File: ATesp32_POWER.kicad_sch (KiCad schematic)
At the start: 17 parts, among them J1 USB_C_Receptacle_USB2.0_16P, J2 JST PH, Q1 DMP2045U, U3 MCP73831-2-OT, U4 AP2112K-3.3

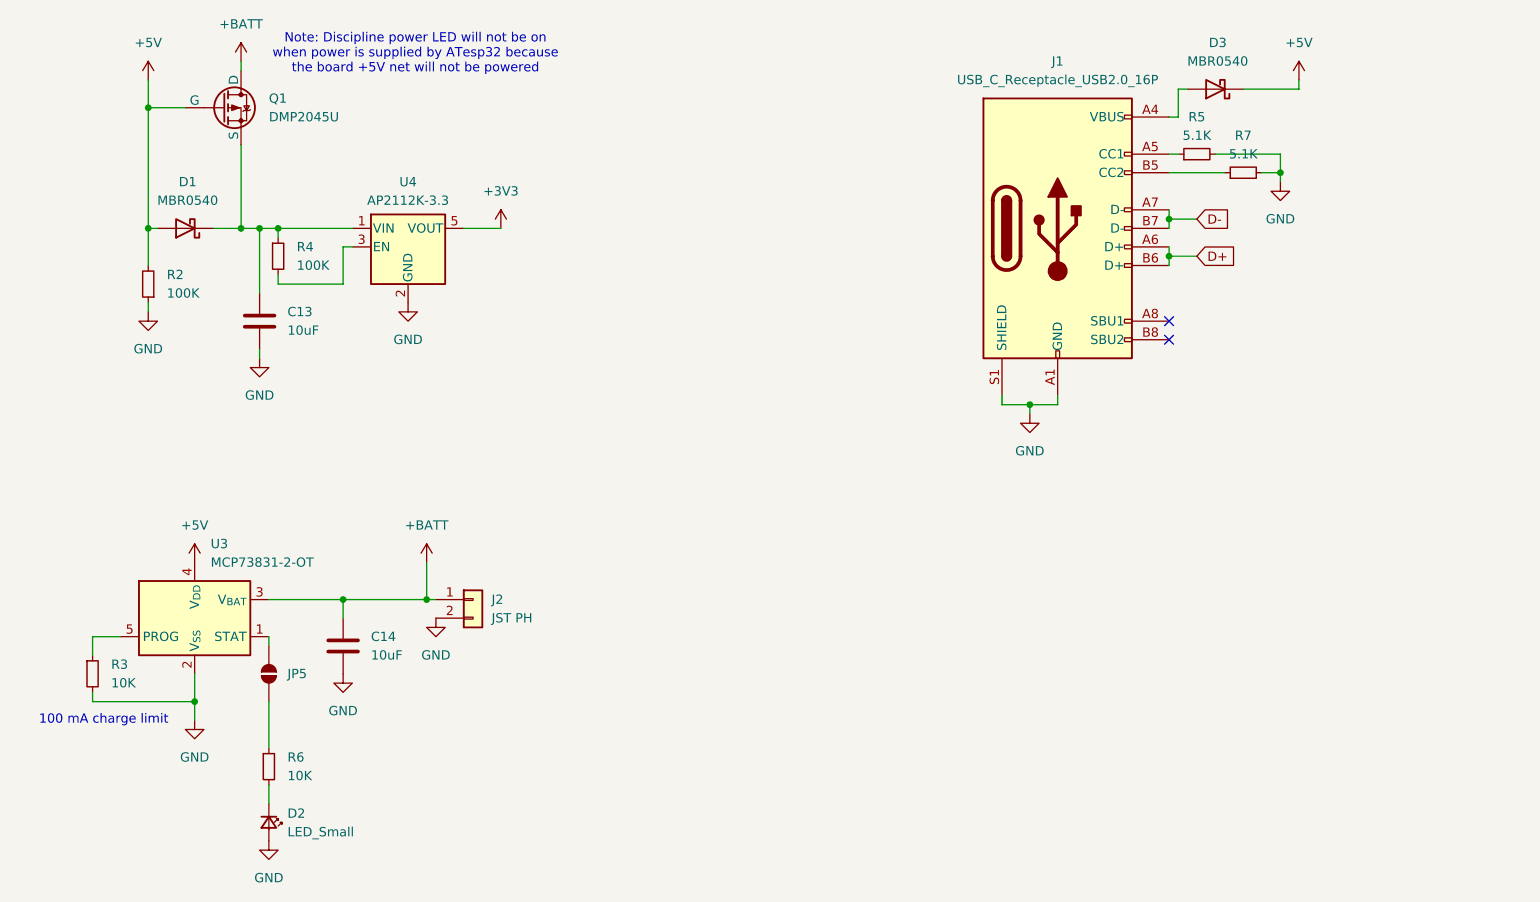
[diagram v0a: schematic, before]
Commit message: Added USB-UART bridge for programming
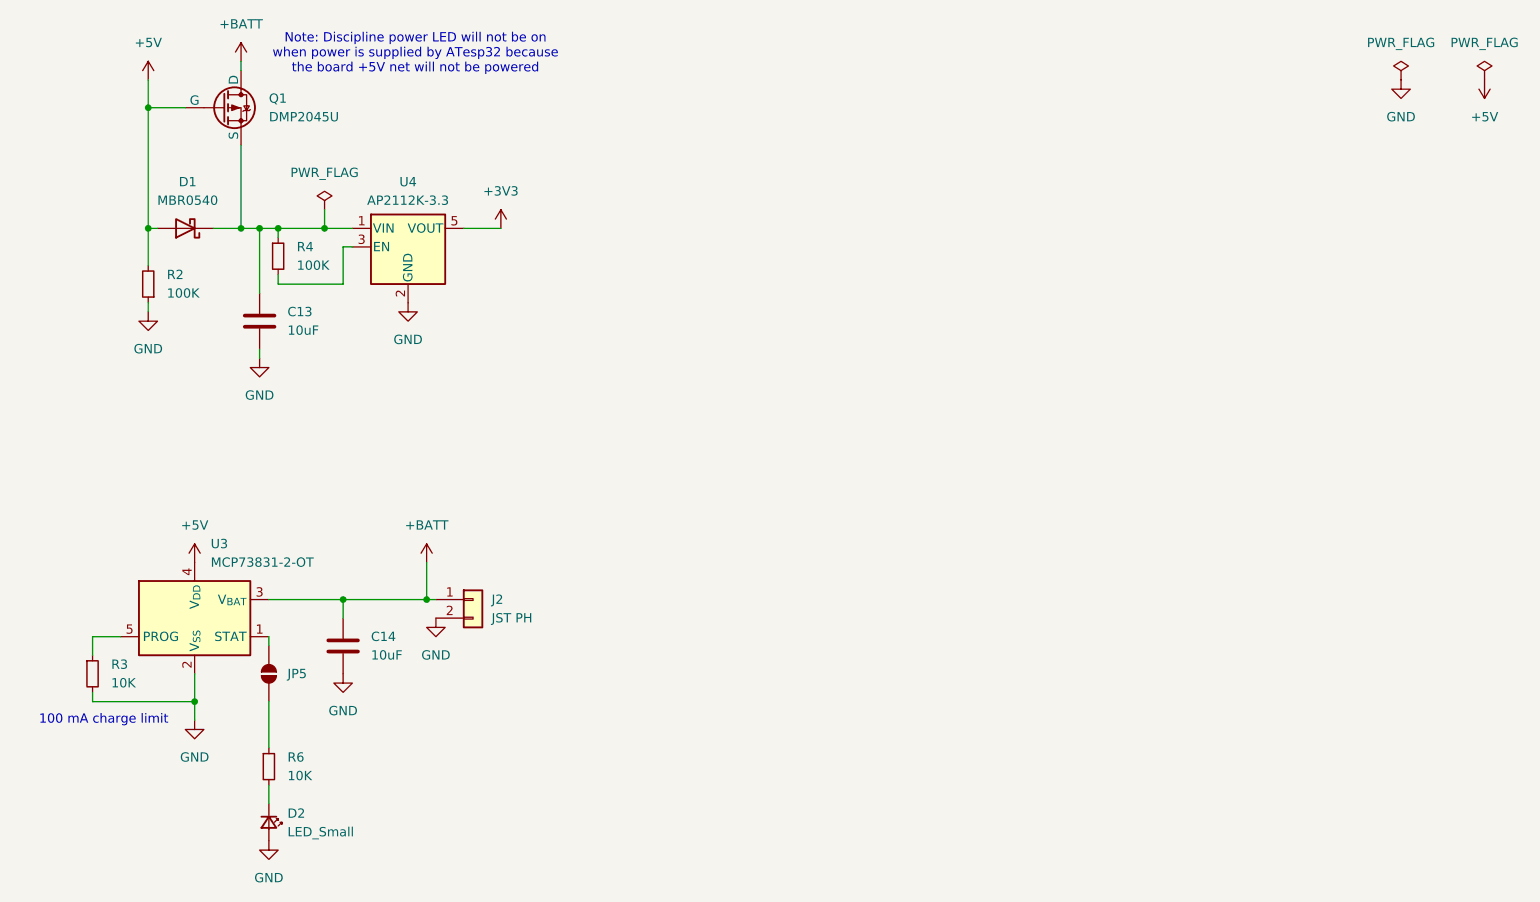
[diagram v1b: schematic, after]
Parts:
- removed D3: MBR0540, Diode_SMD:D_SOD-123, symbol Diode:MBR0540
- removed J1: USB_C_Receptacle_USB2.0_16P, symbol Connector:USB_C_Receptacle_USB2.0_16P
- removed R5, R7: 5.1K, symbol Device:R_Small
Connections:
- no-connect marks 2 -> 0

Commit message: first pass at footprint assignment
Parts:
- C13, C14: footprint (none) -> Capacitor_SMD:C_0603_1608Metric
- D2: footprint (none) -> LED_SMD:LED_0603_1608Metric
- J2: footprint (none) -> Connector_JST:JST_PH_B2B-PH-K_1x02_P2.00mm_Vertical
- JP5: footprint (none) -> Jumper:SolderJumper-2_P1.3mm_Open_RoundedPad1.0x1.5mm
- Q1: footprint (none) -> Package_TO_SOT_SMD:SOT-23
- R2, R3, R4, R6: footprint (none) -> Resistor_SMD:R_0603_1608Metric
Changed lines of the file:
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@@
 			)
 		)
-		(property "Footprint" ""
+		(property "Footprint" "LED_SMD:LED_0603_1608Metric"
 			(at 99.06 152.4 90)
 			(effects
@@
 			)
 		)
-		(property "Footprint" ""
+		(property "Footprint" "Capacitor_SMD:C_0603_1608Metric"
 			(at 98.7552 87.63 0)
 			(effects
@@
 			)
 		)
-		(property "Footprint" ""
+		(property "Footprint" "Capacitor_SMD:C_0603_1608Metric"
 			(at 110.1852 132.08 0)
 			(effects
@@
 			)
 		)
-		(property "Footprint" ""
+		(property "Footprint" "Resistor_SMD:R_0603_1608Metric"
 			(at 99.06 144.78 0)
 			(effects
@@
 			)
 		)
-		(property "Footprint" ""
+		(property "Footprint" "Resistor_SMD:R_0603_1608Metric"
 			(at 74.93 132.08 0)
 			(effects
@@
 			)
 		)
-		(property "Footprint" ""
+		(property "Footprint" "Jumper:SolderJumper-2_P1.3mm_Open_RoundedPad1.0x1.5mm"
 			(at 99.06 132.08 0)
 			(effects
@@
 			)
 		)
-		(property "Footprint" ""
+		(property "Footprint" "Resistor_SMD:R_0603_1608Metric"
 			(at 100.33 74.93 0)
 			(effects
@@
 			)
 		)
-		(property "Footprint" ""
+		(property "Footprint" "Resistor_SMD:R_0603_1608Metric"
 			(at 82.55 78.74 0)
 			(effects
@@
 			)
 		)
-		(property "Footprint" ""
+		(property "Footprint" "Connector_JST:JST_PH_B2B-PH-K_1x02_P2.00mm_Vertical"
 			(at 127 121.92 0)
 			(effects
@@
 			)
 		)
-		(property "Footprint" ""
+		(property "Footprint" "Package_TO_SOT_SMD:SOT-23"
 			(at 97.79 52.07 0)
 			(effects

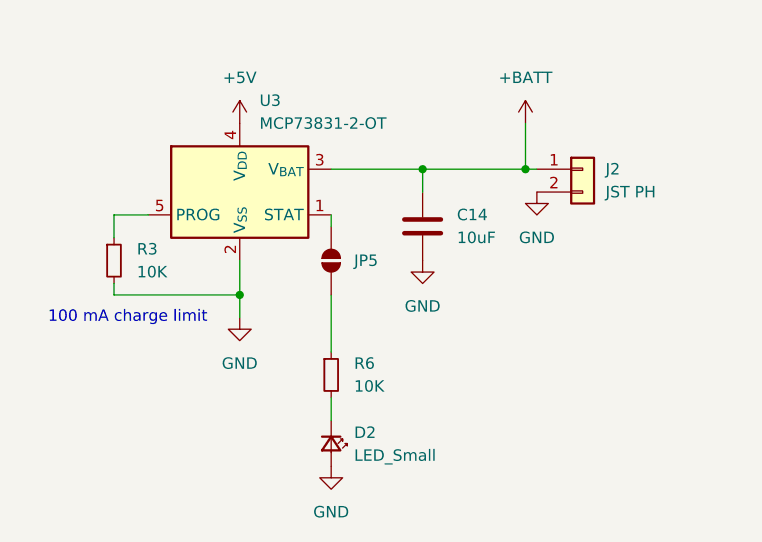
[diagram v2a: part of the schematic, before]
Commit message: remove misc superfluous components
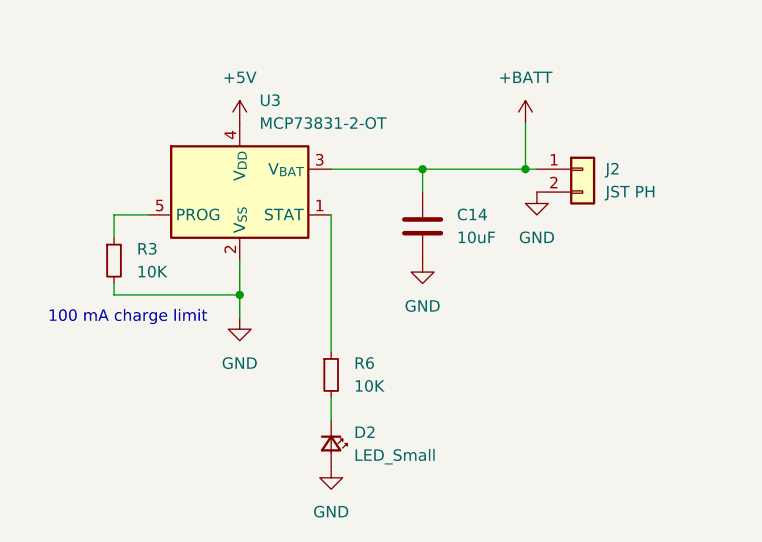
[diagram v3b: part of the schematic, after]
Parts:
- removed JP5: SolderJumper_2_Open, Jumper:SolderJumper-2_P1.3mm_Open_RoundedPad1.0x1.5mm, symbol Jumper:SolderJumper_2_Open
- C13, C14: footprint Capacitor_SMD:C_0603_1608Metric -> Capacitor_SMD:C_0402_1005Metric
- D2: footprint LED_SMD:LED_0603_1608Metric -> LED_SMD:LED_0402_1005Metric
- J2: footprint Connector_JST:JST_PH_B2B-PH-K_1x02_P2.00mm_Vertical -> Connector_JST:JST_PH_S2B-PH-SM4-TB_1x02-1MP_P2.00mm_Horizontal
- R2, R3, R4, R6: footprint Resistor_SMD:R_0603_1608Metric -> Resistor_SMD:R_0402_1005Metric
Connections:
- net at R6.1: now also U3.1 (STAT)
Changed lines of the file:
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@@
 	(wire
 		(pts
-			(xy 99.06 127) (xy 99.06 128.27)
+			(xy 82.55 54.61) (xy 82.55 71.12)
 		)
 		(stroke
@@
 	(wire
 		(pts
-			(xy 82.55 54.61) (xy 82.55 71.12)
-		)
-		(stroke
-			(width 0)
-			(type default)
-		)
-	)
-	(wire
-		(pts
-			(xy 99.06 135.89) (xy 99.06 142.24)
+			(xy 99.06 127) (xy 99.06 142.24)
 		)
 		(stroke
@@
 			)
 		)
-		(property "Footprint" "LED_SMD:LED_0603_1608Metric"
+		(property "Footprint" "LED_SMD:LED_0402_1005Metric"
 			(at 99.06 152.4 90)
 			(effects
@@
 			)
 		)
-		(property "Footprint" "Capacitor_SMD:C_0603_1608Metric"
+		(property "Footprint" "Capacitor_SMD:C_0402_1005Metric"
 			(at 98.7552 87.63 0)
 			(effects
@@
 			)
 		)
-		(property "Footprint" "Capacitor_SMD:C_0603_1608Metric"
+		(property "Footprint" "Capacitor_SMD:C_0402_1005Metric"
 			(at 110.1852 132.08 0)
 			(effects
@@
 			)
 		)
-		(property "Footprint" "Resistor_SMD:R_0603_1608Metric"
+		(property "Footprint" "Resistor_SMD:R_0402_1005Metric"
 			(at 99.06 144.78 0)
 			(effects
@@
 			)
 		)
-		(property "Footprint" "Resistor_SMD:R_0603_1608Metric"
+		(property "Footprint" "Resistor_SMD:R_0402_1005Metric"
 			(at 74.93 132.08 0)
 			(effects
@@
 	)
 	(symbol
-		(lib_id "Jumper:SolderJumper_2_Open")
-		(at 99.06 132.08 90)
-		(unit 1)
-		(exclude_from_sim yes)
-		(in_bom no)
-		(on_board yes)
-		(dnp no)
-		(fields_autoplaced yes)
-		(property "Reference" "JP5"
-			(at 101.6 132.0799 90)
-			(effects
-				(font
-					(size 1.27 1.27)
-				)
-				(justify right)
-			)
-		)
-		(property "Value" "SolderJumper_2_Open"
-			(at 95.25 132.08 0)
-			(effects
-				(font
-					(size 1.27 1.27)
-				)
-				(hide yes)
-			)
-		)
-		(property "Footprint" "Jumper:SolderJumper-2_P1.3mm_Open_RoundedPad1.0x1.5mm"
-			(at 99.06 132.08 0)
-			(effects
-				(font
-					(size 1.27 1.27)
-				)
-				(hide yes)
-			)
-		)
-		(property "Datasheet" "~"
-			(at 99.06 132.08 0)
-			(effects
-				(font
-					(size 1.27 1.27)
-				)
-				(hide yes)
-			)
-		)
-		(property "Description" "Solder Jumper, 2-pole, open"
-			(at 99.06 132.08 0)
-			(effects
-				(font
-					(size 1.27 1.27)
-				)
-				(hide yes)
-			)
-		)
-		(pin "2"
-		)
-		(pin "1"
-		)
-		(instances
-			(project "ATesp32"
-				(path "/465ced44-ee36-4323-9fa6-a4501ea89ff6/2df8408e-27a9-477c-88a6-1eead4d75269"
-					(reference "JP5")
-					(unit 1)
-				)
-			)
-		)
-	)
-	(symbol
 		(lib_id "power:+5V")
 		(at 88.9 116.84 0)
@@
 			)
 		)
-		(property "Footprint" "Resistor_SMD:R_0603_1608Metric"
+		(property "Footprint" "Resistor_SMD:R_0402_1005Metric"
 			(at 100.33 74.93 0)
 			(effects
@@
 			)
 		)
-		(property "Footprint" "Resistor_SMD:R_0603_1608Metric"
+		(property "Footprint" "Resistor_SMD:R_0402_1005Metric"
 			(at 82.55 78.74 0)
 			(effects
@@
 			)
 		)
-		(property "Footprint" "Connector_JST:JST_PH_B2B-PH-K_1x02_P2.00mm_Vertical"
+		(property "Footprint" "Connector_JST:JST_PH_S2B-PH-SM4-TB_1x02-1MP_P2.00mm_Horizontal"
 			(at 127 121.92 0)
 			(effects

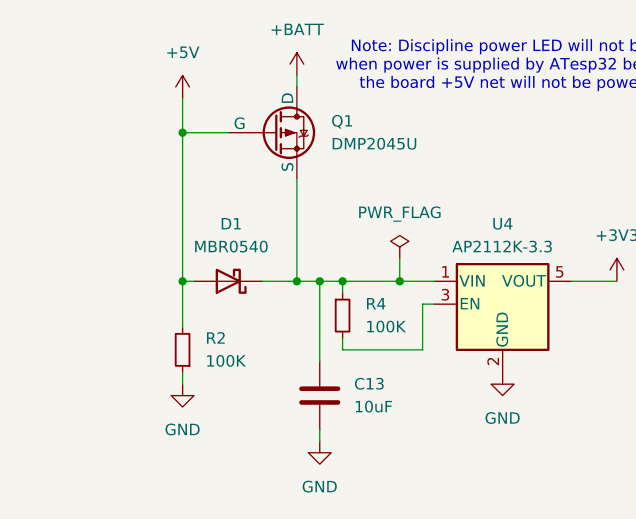
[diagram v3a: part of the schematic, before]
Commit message: first pass at component placement
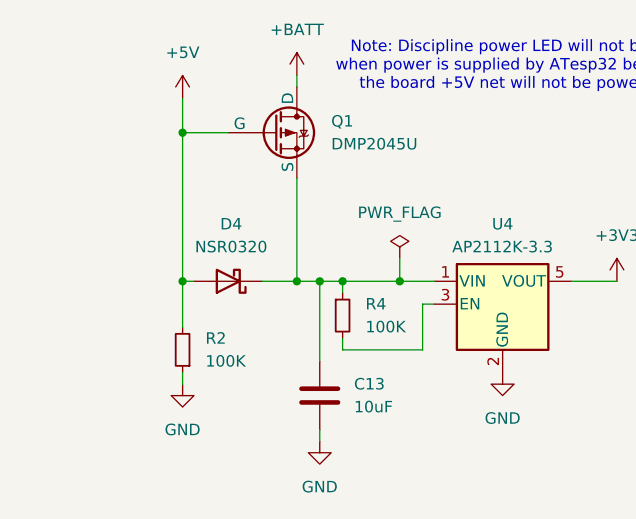
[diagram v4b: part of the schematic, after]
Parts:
- removed D1: MBR0540, Diode_SMD:D_SOD-123, symbol Diode:MBR0540
- added D4: NSR0320, Diode_SMD:D_SOD-323, symbol Diode:NSR0340HT1G
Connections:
- net +5V: now also D4.2 (A)
- net at C13.1, Q1.3 (S), R4.1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: now also D4.1 (K)
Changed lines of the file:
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@@
-	)
-	(symbol
-		(lib_id "Diode:MBR0540")
-		(at 87.63 71.12 180)
-		(unit 1)
-		(exclude_from_sim no)
-		(in_bom yes)
-		(on_board yes)
-		(dnp no)
-		(fields_autoplaced yes)
-		(property "Reference" "D1"
-			(at 87.9475 64.77 0)
-			(effects
-				(font
-					(size 1.27 1.27)
-				)
-			)
-		)
-		(property "Value" "MBR0540"
-			(at 87.9475 67.31 0)
-			(effects
-				(font
-					(size 1.27 1.27)
-				)
-			)
-		)
-		(property "Footprint" "Diode_SMD:D_SOD-123"
-			(at 87.63 66.675 0)
-			(effects
-				(font
-					(size 1.27 1.27)
-				)
-				(hide yes)
-			)
-		)
-		(property "Datasheet" "http://www.mccsemi.com/up_pdf/MBR0520~MBR0580(SOD123).pdf"
-			(at 87.63 71.12 0)
-			(effects
-				(font
-					(size 1.27 1.27)
-				)
-				(hide yes)
-			)
-		)
-		(property "Description" "40V 0.5A Schottky Power Rectifier Diode, SOD-123"
-			(at 87.63 71.12 0)
-			(effects
-				(font
-					(size 1.27 1.27)
-				)
-				(hide yes)
-			)
-		)
-		(pin "1"
-		)
-		(pin "2"
-		)
-		(instances
-			(project "ATesp32"
-				(path "/465ced44-ee36-4323-9fa6-a4501ea89ff6/2df8408e-27a9-477c-88a6-1eead4d75269"
-					(reference "D1")
-					(unit 1)
-				)
-			)
-		)
 	)
 	(symbol
@@
 					(unit 1)
 				)
+			)
+		)
+	)
+	(symbol
+		(lib_id "Diode:NSR0340HT1G")
+		(at 87.63 71.12 180)
+		(unit 1)
+		(exclude_from_sim no)
+		(in_bom yes)
+		(on_board yes)
+		(dnp no)
+		(fields_autoplaced yes)
+		(property "Reference" "D4"
+			(at 87.9475 64.77 0)
+			(effects
+				(font
+					(size 1.27 1.27)
+				)
+			)
+		)
+		(property "Value" "NSR0320"
+			(at 87.9475 67.31 0)
+			(effects
+				(font
+					(size 1.27 1.27)
+				)
+			)
+		)
+		(property "Footprint" "Diode_SMD:D_SOD-323"
+			(at 87.63 66.675 0)
+			(effects
+				(font
+					(size 1.27 1.27)
+				)
+				(hide yes)
+			)
+		)
+		(property "Datasheet" "https://www.onsemi.com/pdf/datasheet/nsr0320mw2t1-d.pdf"
+			(at 87.63 71.12 0)
+			(effects
+				(font
+					(size 1.27 1.27)
+				)
+				(hide yes)
+			)
+		)
+		(property "Description" "20V 1A Schottky Diode, SOD-323"
+			(at 87.63 71.12 0)
+			(effects
+				(font
+					(size 1.27 1.27)
+				)
+				(hide yes)
+			)
+		)
+		(pin "2"
+		)
+		(pin "1"
+		)
+		(instances
+			(project ""
+				(path "/465ced44-ee36-4323-9fa6-a4501ea89ff6/2df8408e-27a9-477c-88a6-1eead4d75269"
+					(reference "D4")
+					(unit 1)
+				)

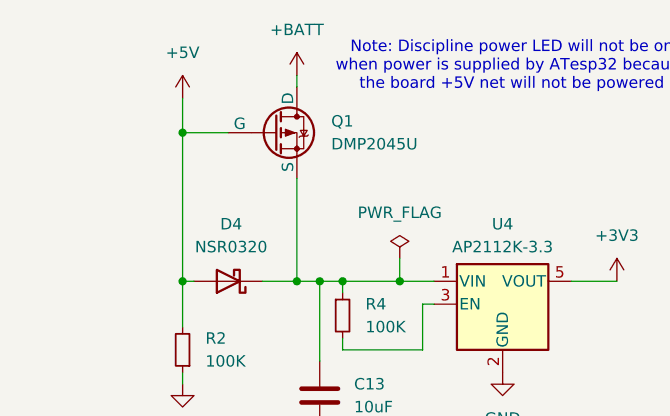
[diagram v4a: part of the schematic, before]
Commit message: critical error - changed to correct mosfet pin numbers
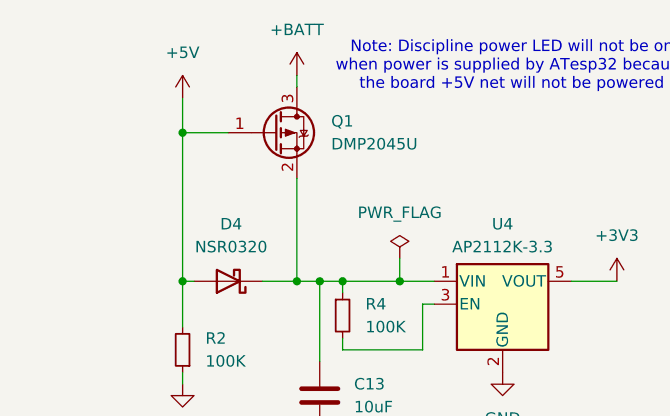
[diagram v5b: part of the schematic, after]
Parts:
- removed Q1: DMP2045U, Package_TO_SOT_SMD:SOT-23, symbol Simulation_SPICE:PMOS
- added Q1: DMP2045U, Package_TO_SOT_SMD:SOT-23, symbol Device:Q_PMOS_GSD
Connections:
- net +5V: now also Q1.1 (G)
- net +BATT: now also Q1.3 (D)
- net at C13.1, D4.1 (K), R4.1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: now also Q1.2 (S)
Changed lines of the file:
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@@
+	)
+	(symbol
+		(lib_id "Device:Q_PMOS_GSD")
+		(at 92.71 54.61 0)
+		(unit 1)
+		(exclude_from_sim no)
+		(in_bom yes)
+		(on_board yes)
+		(dnp no)
+		(fields_autoplaced yes)
+		(property "Reference" "Q1"
+			(at 99.06 53.3399 0)
+			(effects
+				(font
+					(size 1.27 1.27)
+				)
+				(justify left)
+			)
+		)
+		(property "Value" "DMP2045U"
+			(at 99.06 55.8799 0)
+			(effects
+				(font
+					(size 1.27 1.27)
+				)
+				(justify left)
+			)
+		)
+		(property "Footprint" "Package_TO_SOT_SMD:SOT-23"
+			(at 97.79 52.07 0)
+			(effects
+				(font
+					(size 1.27 1.27)
+				)
+				(hide yes)
+			)
+		)
+		(property "Datasheet" "https://www.diodes.com/assets/Datasheets/DMP2045U.pdf"
+			(at 92.71 54.61 0)
+			(effects
+				(font
+					(size 1.27 1.27)
+				)
+				(hide yes)
+			)
+		)
+		(property "Description" "P-MOSFET transistor, gate/source/drain"
+			(at 92.71 54.61 0)
+			(effects
+				(font
+					(size 1.27 1.27)
+				)
+				(hide yes)
+			)
+		)
+		(pin "3"
+		)
+		(pin "2"
+		)
+		(pin "1"
+		)
+		(instances
+			(project ""
+				(path "/465ced44-ee36-4323-9fa6-a4501ea89ff6/2df8408e-27a9-477c-88a6-1eead4d75269"
+					(reference "Q1")
+					(unit 1)
+				)
+			)
+		)
 	)
 	(symbol
@@
 					(unit 1)
 				)
-			)
-		)
-	)
-	(symbol
-		(lib_id "Simulation_SPICE:PMOS")
-		(at 92.71 54.61 0)
-		(unit 1)
-		(exclude_from_sim no)
-		(in_bom yes)
-		(on_board yes)
-		(dnp no)
-		(fields_autoplaced yes)
-		(property "Reference" "Q1"
-			(at 99.06 53.3399 0)
-			(effects
-				(font
-					(size 1.27 1.27)
-				)
-				(justify left)
-			)
-		)
-		(property "Value" "DMP2045U"
-			(at 99.06 55.8799 0)
-			(effects
-				(font
-					(size 1.27 1.27)
-				)
-				(justify left)
-			)
-		)
-		(property "Footprint" "Package_TO_SOT_SMD:SOT-23"
-			(at 97.79 52.07 0)
-			(effects
-				(font
-					(size 1.27 1.27)
-				)
-				(hide yes)
-			)
-		)
-		(property "Datasheet" "https://ngspice.sourceforge.io/docs/ngspice-html-manual/manual.xhtml#cha_MOSFETs"
-			(at 92.71 67.31 0)
-			(effects
-				(font
-					(size 1.27 1.27)
-				)
-				(hide yes)
-			)
-		)
-		(property "Description" "P-MOSFET transistor, drain/source/gate"
-			(at 92.71 54.61 0)
-			(effects
-				(font
-					(size 1.27 1.27)
-				)
-				(hide yes)
-			)
-		)
-		(property "Sim.Device" "PMOS"
-			(at 92.71 71.755 0)
-			(effects
-				(font
-					(size 1.27 1.27)
-				)
-				(hide yes)
-			)
-		)
-		(property "Sim.Type" "VDMOS"
-			(at 92.71 73.66 0)
-			(effects
-				(font
-					(size 1.27 1.27)
-				)
-				(hide yes)
-			)
-		)
-		(property "Sim.Pins" "1=D 2=G 3=S"
-			(at 92.71 69.85 0)
-			(effects
-				(font
-					(size 1.27 1.27)
-				)
-				(hide yes)
-			)
-		)
-		(pin "3"
-		)
-		(pin "2"
-		)
-		(pin "1"
-		)
-		(instances
-			(project "ATesp32"
-				(path "/465ced44-ee36-4323-9fa6-a4501ea89ff6/2df8408e-27a9-477c-88a6-1eead4d75269"
-					(reference "Q1")
-					(unit 1)
-				)
